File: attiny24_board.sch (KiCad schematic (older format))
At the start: 11 parts, among them J1 SPI, J2 OUT, J3 SCKLED, J4 CONN_01X02, U1 ATTINY24A-SSU, Y1 12000

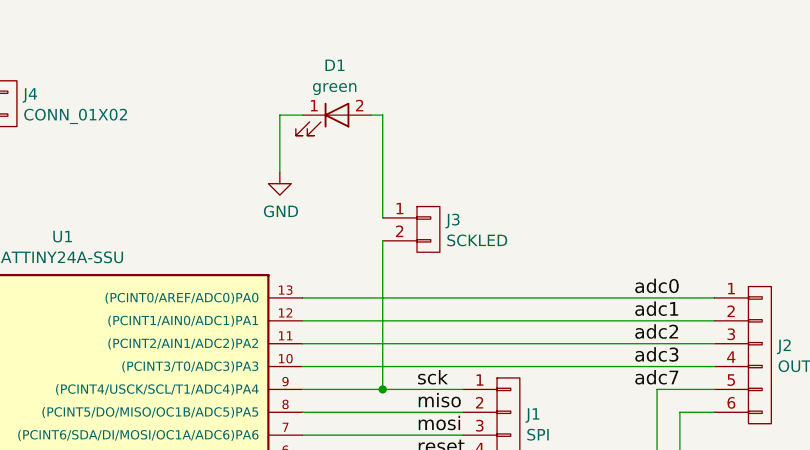
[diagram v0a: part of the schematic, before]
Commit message: Add forgoteen resistor
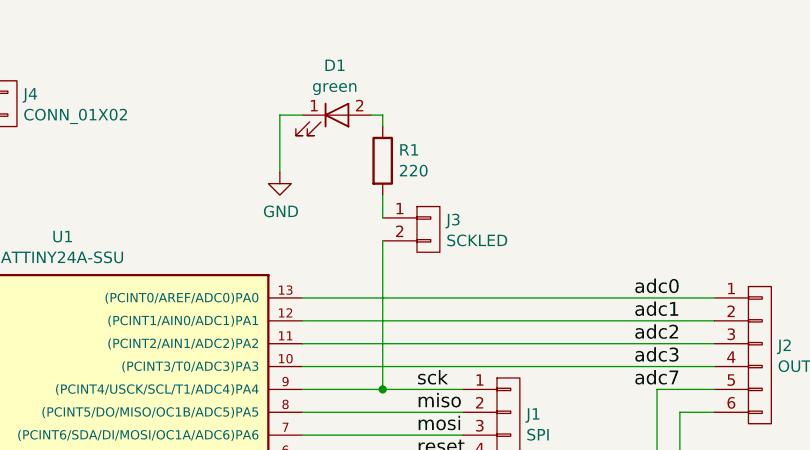
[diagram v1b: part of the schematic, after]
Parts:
- added R1: 220, symbol R
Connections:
- net at J3.1 (P1): now also R1.2; no longer D1.2 (A)
- new net: D1.2 (A), R1.1
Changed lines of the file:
@@
 $EndComp
 $Comp
-L +3.3V #PWR01
+L +3.3V #PWR1
 U 1 1 59371D88
 P 3150 2800
-F 0 "#PWR01" H 3150 2650 50  0001 C CNN
+F 0 "#PWR1" H 3150 2650 50  0001 C CNN
 F 1 "+3.3V" H 3165 2973 50  0000 C CNN
 F 2 "" H 3150 2800 50  0001 C CNN
@@
 	3150 2800 3150 3100
 $Comp
-L GND #PWR02
+L GND #PWR2
 U 1 1 59371F04
 P 3150 3400
-F 0 "#PWR02" H 3150 3150 50  0001 C CNN
+F 0 "#PWR2" H 3150 3150 50  0001 C CNN
 F 1 "GND" H 3155 3227 50  0000 C CNN
 F 2 "" H 3150 3400 50  0001 C CNN
@@
 $EndComp
 $Comp
-L GND #PWR03
+L GND #PWR3
 U 1 1 59371F1C
 P 3650 3400
-F 0 "#PWR03" H 3650 3150 50  0001 C CNN
+F 0 "#PWR3" H 3650 3150 50  0001 C CNN
 F 1 "GND" H 3655 3227 50  0000 C CNN
 F 2 "" H 3650 3400 50  0001 C CNN
@@
 $EndComp
 $Comp
-L GND #PWR04
+L GND #PWR4
 U 1 1 59371F48
 P 3900 4250
-F 0 "#PWR04" H 3900 4000 50  0001 C CNN
+F 0 "#PWR4" H 3900 4000 50  0001 C CNN
 F 1 "GND" H 3905 4077 50  0000 C CNN
 F 2 "" H 3900 4250 50  0001 C CNN
@@
 	7200 3900 7200 4550
 $Comp
-L GND #PWR05
+L GND #PWR8
 U 1 1 593738FE
 P 6700 4850
-F 0 "#PWR05" H 6700 4600 50  0001 C CNN
+F 0 "#PWR8" H 6700 4600 50  0001 C CNN
 F 1 "GND" H 6705 4677 50  0000 C CNN
 F 2 "" H 6700 4850 50  0001 C CNN
@@
 $EndComp
 $Comp
-L GND #PWR06
+L GND #PWR9
 U 1 1 5937391E
 P 7200 4850
-F 0 "#PWR06" H 7200 4600 50  0001 C CNN
+F 0 "#PWR9" H 7200 4600 50  0001 C CNN
 F 1 "GND" H 7205 4677 50  0000 C CNN
 F 2 "" H 7200 4850 50  0001 C CNN
@@
 $EndComp
 $Comp
-L GND #PWR07
+L GND #PWR7
 U 1 1 5937437A
 P 6000 2450
-F 0 "#PWR07" H 6000 2200 50  0001 C CNN
+F 0 "#PWR7" H 6000 2200 50  0001 C CNN
 F 1 "GND" H 6005 2277 50  0000 C CNN
 F 2 "" H 6000 2450 50  0001 C CNN
@@
 Wire Wire Line
 	6400 2200 6450 2200
-Wire Wire Line
-	6450 2200 6450 2650
 Wire Wire Line
 	6100 2200 6000 2200
@@
 $EndComp
 $Comp
-L GND #PWR08
+L GND #PWR6
 U 1 1 59374F93
 P 4500 2300
-F 0 "#PWR08" H 4500 2050 50  0001 C CNN
+F 0 "#PWR6" H 4500 2050 50  0001 C CNN
 F 1 "GND" H 4505 2127 50  0000 C CNN
 F 2 "" H 4500 2300 50  0001 C CNN
@@
 	4500 2200 4500 2300
 $Comp
-L +3.3V #PWR09
+L +3.3V #PWR5
 U 1 1 59374FE5
 P 4500 2000
-F 0 "#PWR09" H 4500 1850 50  0001 C CNN
+F 0 "#PWR5" H 4500 1850 50  0001 C CNN
 F 1 "+3.3V" H 4515 2173 50  0000 C CNN
 F 2 "" H 4500 2000 50  0001 C CNN
@@
 Connection ~ 3150 3000
 $Comp
-L PWR_FLAG #FLG?
+L PWR_FLAG #FLG1
 U 1 1 593754B4
 P 2850 2450
-F 0 "#FLG?" H 2850 2525 50  0001 C CNN
+F 0 "#FLG1" H 2850 2525 50  0001 C CNN
 F 1 "PWR_FLAG" H 2850 2624 50  0000 C CNN
 F 2 "" H 2850 2450 50  0001 C CNN
@@
 Connection ~ 3150 2850
 $Comp
-L PWR_FLAG #FLG?
+L PWR_FLAG #FLG2
 U 1 1 59375515
 P 4150 2050
-F 0 "#FLG?" H 4150 2125 50  0001 C CNN
+F 0 "#FLG2" H 4150 2125 50  0001 C CNN
 F 1 "PWR_FLAG" H 4150 2224 50  0000 C CNN
 F 2 "" H 4150 2050 50  0001 C CNN
@@
 Wire Wire Line
 	4150 2300 4150 2050
+$Comp
+L R R1
+U 1 1 5939A84A
+P 6450 2400
+F 0 "R1" H 6520 2446 50  0000 L CNN
+F 1 "220" H 6520 2355 50  0000 L CNN
+F 2 "" V 6380 2400 50  0001 C CNN
+F 3 "" H 6450 2400 50  0001 C CNN
+	1    6450 2400
+	1    0    0    -1
+$EndComp
+Wire Wire Line
+	6450 2200 6450 2250
+Wire Wire Line
+	6450 2550 6450 2650
 $EndSCHEMATC
